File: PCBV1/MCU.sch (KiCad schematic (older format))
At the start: 42 parts, among them J4 M50-3610742, U4 STM32F469IITx, X1 ECS-5032MV-100-CN-TR

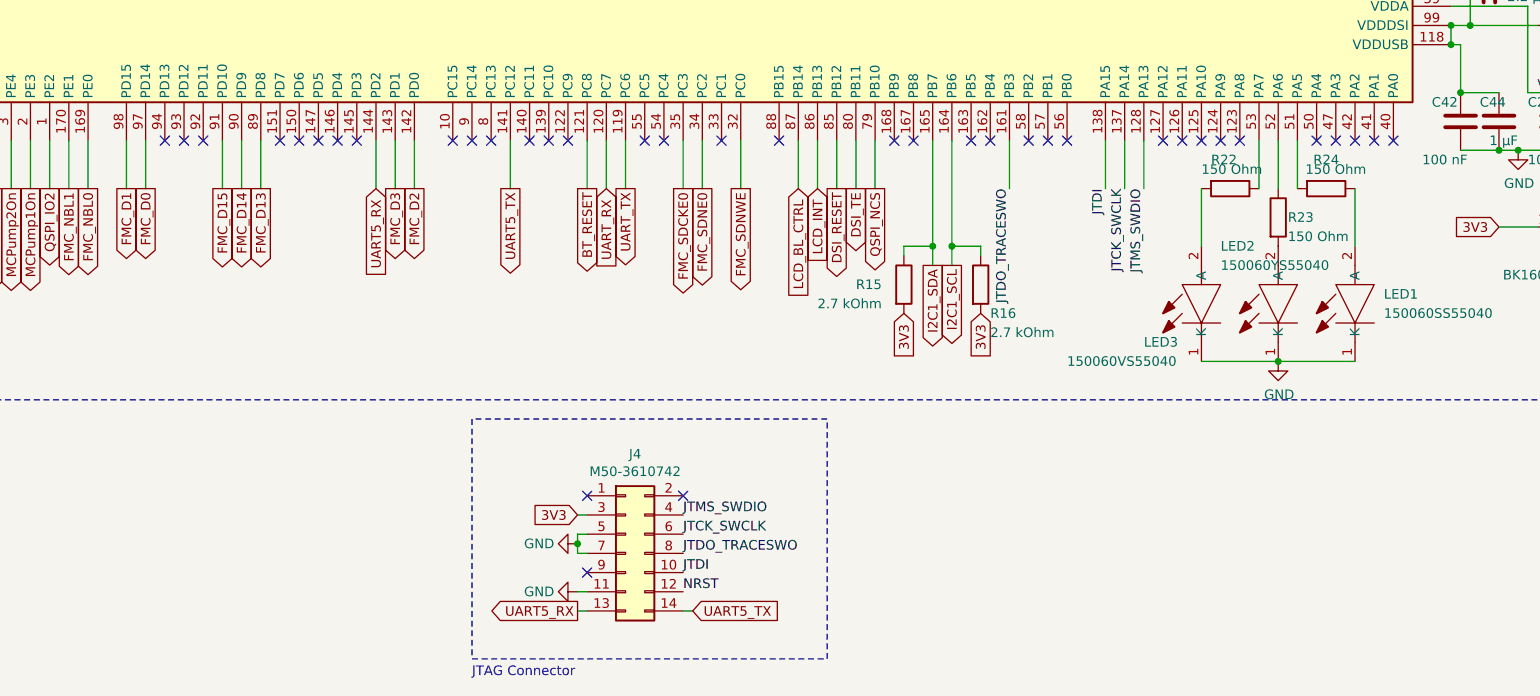
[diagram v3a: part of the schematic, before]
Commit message: Fixed FMC related error in MX file and added ADC pin. Added connector and filter for external sensor.
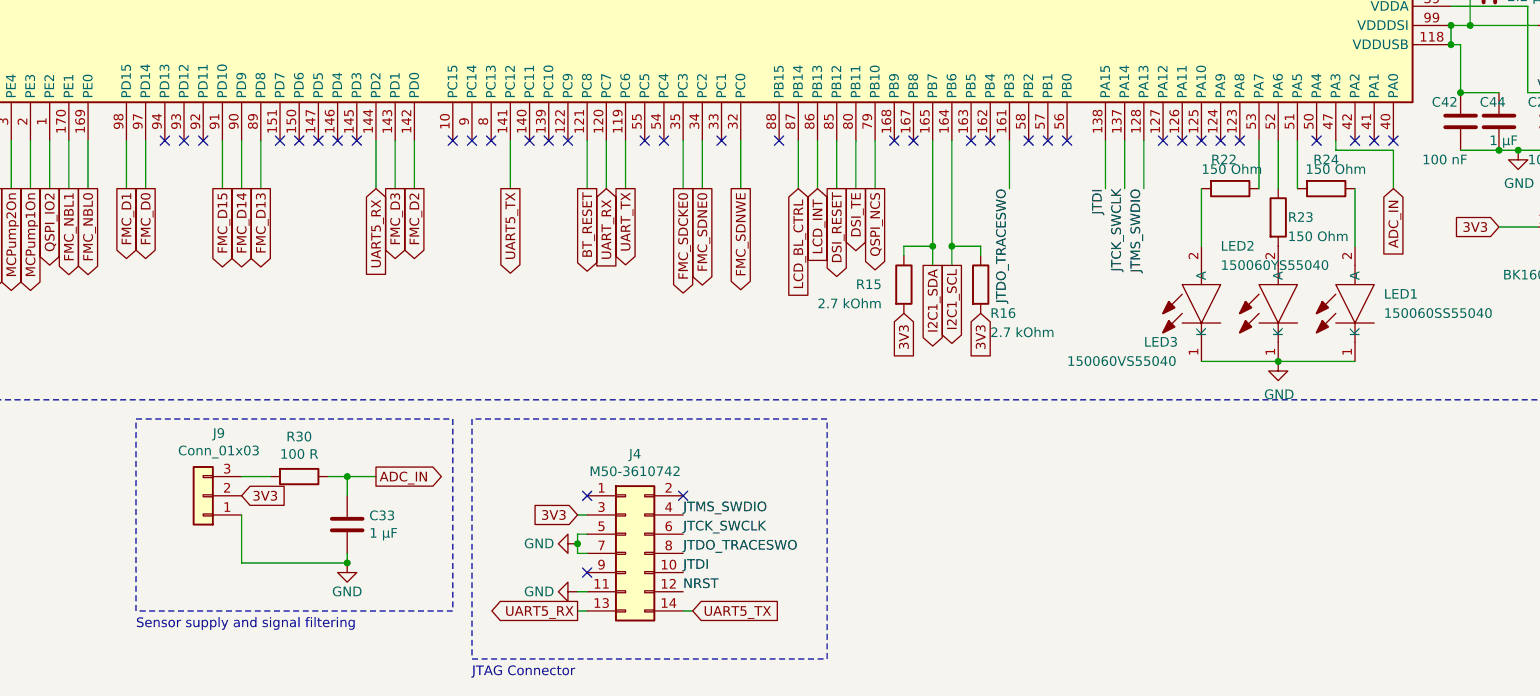
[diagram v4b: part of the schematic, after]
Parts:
- added C33: 1 µF, Capacitor_SMD:C_0603_1608Metric, symbol Device:C
- added J9: Conn_01x03, Connector_PinHeader_2.54mm:PinHeader_1x03_P2.54mm_Vertical, symbol Connector_Generic:Conn_01x03
- added R30: 100 R, Resistor_SMD:R_0603_1608Metric, symbol Device:R
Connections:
- net 3V3: now also J9.2 (Pin_2)
- net GND: now also C33.2, J9.1 (Pin_1)
- net ADC_IN: now reaches U4.47 (PA3)
- net ADC_IN: now also C33.1, R30.1
- new net: J9.3 (Pin_3), R30.2
- no-connect marks 66 -> 65
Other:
- note added: "Sensor supply and signal filtering"
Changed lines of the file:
@@
 NoConn ~ 9700 5000
 NoConn ~ 9600 5000
-NoConn ~ 9500 5000
 NoConn ~ 9400 5000
 NoConn ~ 9000 5000
@@
 	0    -1   -1   0
 $EndComp
+Wire Wire Line
+	9500 5000 9500 5050
+Wire Wire Line
+	9500 5050 9800 5050
+Wire Wire Line
+	9800 5050 9800 5250
+Text GLabel 9800 5250 3    50   Input ~ 0
+ADC_IN
+Text GLabel 4500 6750 2    50   Output ~ 0
+ADC_IN
+$Comp
+L Device:R R30
+U 1 1 5FA5CF0D
+P 4100 6750
+F 0 "R30" V 3893 6750 50  0000 C CNN
+F 1 "100 R" V 3984 6750 50  0000 C CNN
+F 2 "Resistor_SMD:R_0603_1608Metric" V 4030 6750 50  0001 C CNN
+F 3 "~" H 4100 6750 50  0001 C CNN
+	1    4100 6750
+	0    1    1    0
+$EndComp
+$Comp
+L Device:C C33
+U 1 1 5FA5E6B4
+P 4350 7000
+F 0 "C33" H 4465 7046 50  0000 L CNN
+F 1 "1 µF" H 4465 6955 50  0000 L CNN
+F 2 "Capacitor_SMD:C_0603_1608Metric" H 4388 6850 50  0001 C CNN
+F 3 "~" H 4350 7000 50  0001 C CNN
+	1    4350 7000
+	1    0    0    -1
+$EndComp
+Wire Wire Line
+	4250 6750 4350 6750
+Wire Wire Line
+	4350 6750 4350 6850
+Wire Wire Line
+	4500 6750 4350 6750
+Connection ~ 4350 6750
+Wire Wire Line
+	4350 7150 4350 7200
+$Comp
+L power:GND #PWR01
+U 1 1 5FA93D80
+P 4350 7200
+F 0 "#PWR01" H 4350 6950 50  0001 C CNN
+F 1 "GND" H 4350 7050 50  0000 C CNN
+F 2 "" H 4350 7200 50  0001 C CNN
+F 3 "" H 4350 7200 50  0001 C CNN
+	1    4350 7200
+	1    0    0    -1
+$EndComp
+Wire Notes Line
+	3250 6450 4900 6450
+Wire Notes Line
+	4900 6450 4900 7450
+Wire Notes Line
+	4900 7450 3250 7450
+Wire Notes Line
+	3250 7450 3250 6450
+Text Notes 3250 7550 0    50   ~ 0
+Sensor supply and signal filtering
+$Comp
+L Connector_Generic:Conn_01x03 J9
+U 1 1 5FAE963D
+P 3600 6850
+F 0 "J9" H 3518 6525 50  0000 C CNN
+F 1 "Conn_01x03" H 3518 6616 50  0000 C CNN
+F 2 "Connector_PinHeader_2.54mm:PinHeader_1x03_P2.54mm_Vertical" H 3600 6850 50  0001 C CNN
+F 3 "~" H 3600 6850 50  0001 C CNN
+	1    3600 6850
+	-1   0    0    1
+$EndComp
+Wire Wire Line
+	3800 6750 3950 6750
+Text GLabel 3800 6850 2    50   Input ~ 0
+3V3
+Wire Wire Line
+	3800 6950 3800 7200
+Wire Wire Line
+	3800 7200 4350 7200
+Connection ~ 4350 7200
 $EndSCHEMATC
